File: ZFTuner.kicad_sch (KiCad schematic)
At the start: 2 parts, among them J101 RF_In, J102 RF_Out

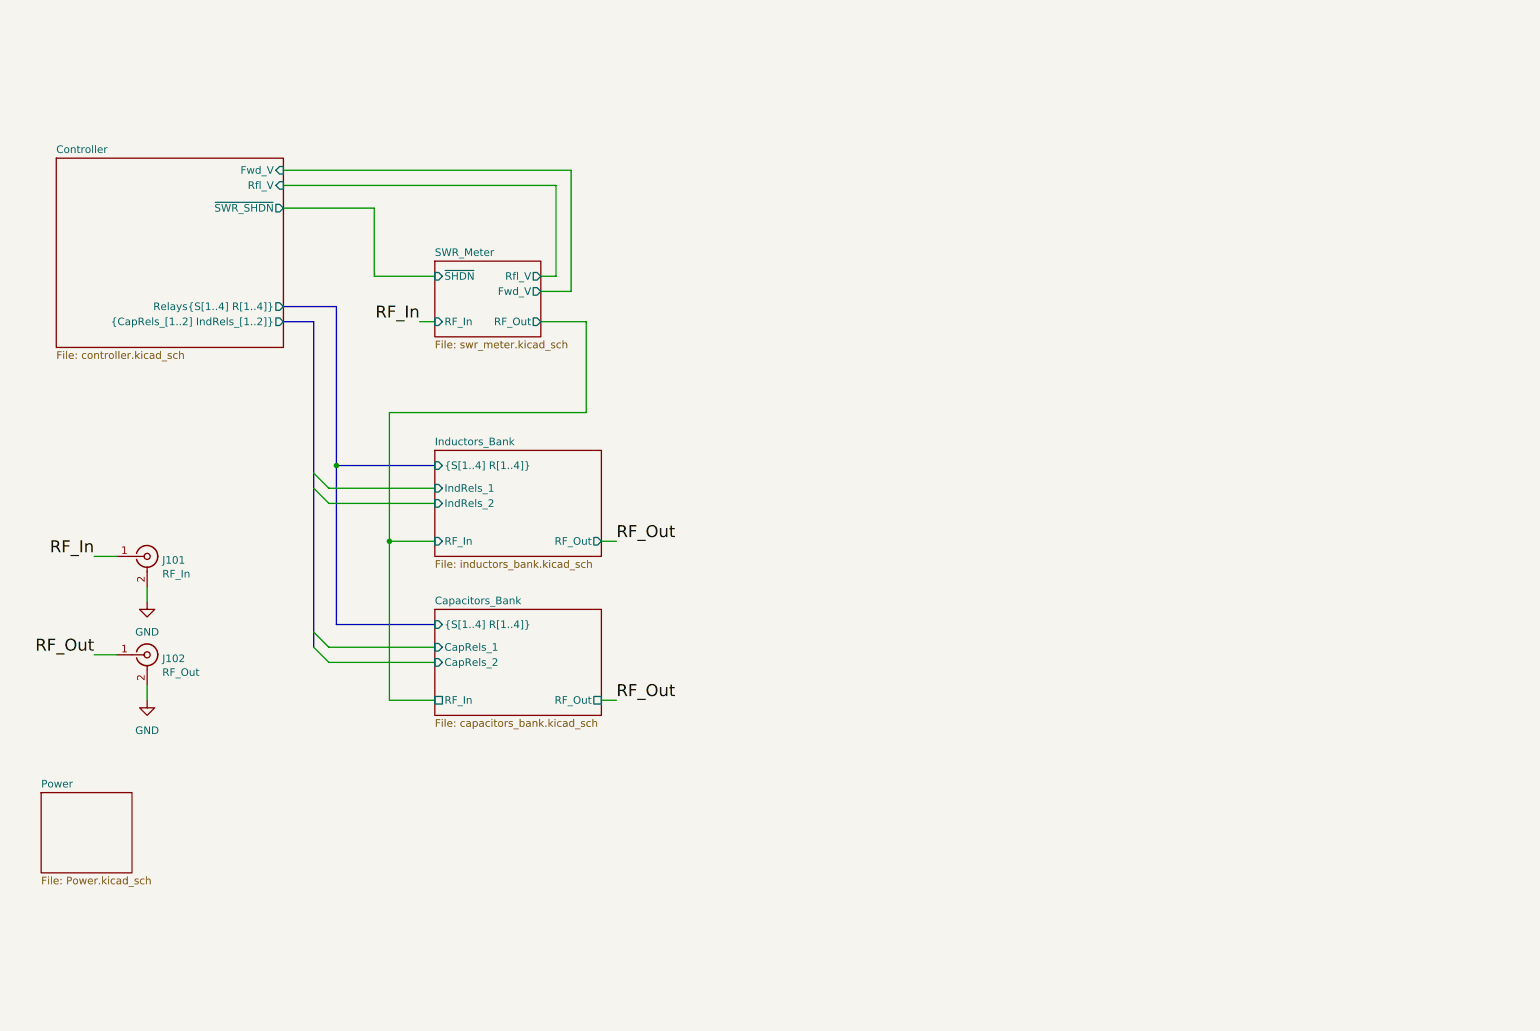
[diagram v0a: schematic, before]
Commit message: Add some missing footprints and rearranged schematics a bit
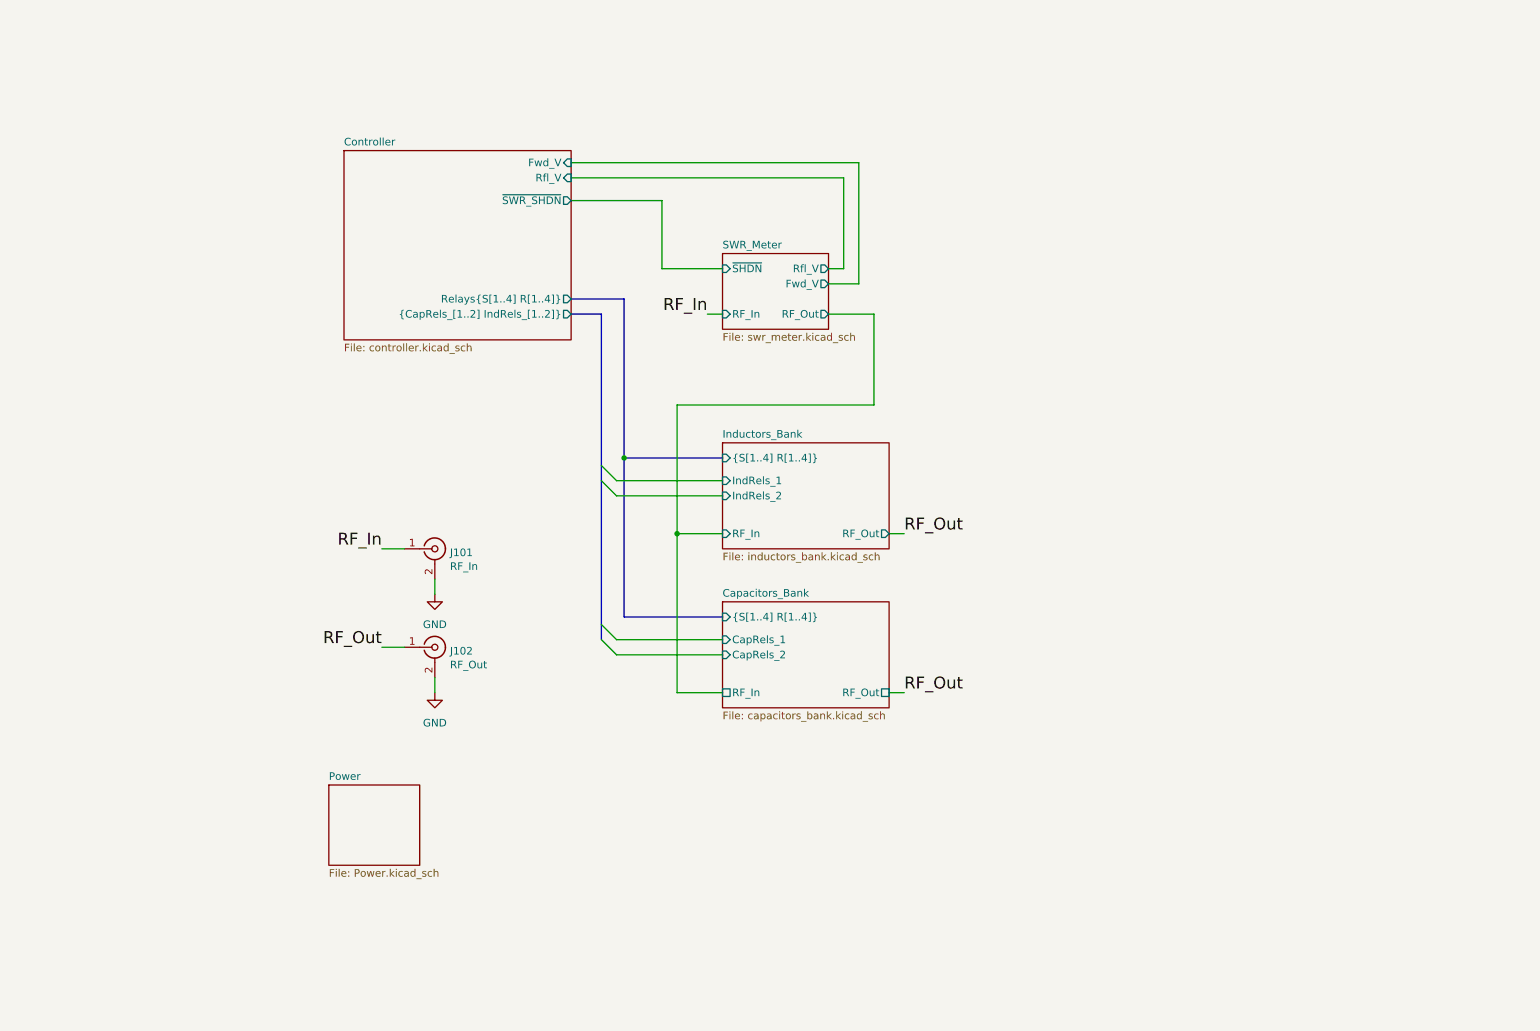
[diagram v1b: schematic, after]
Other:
- moved on the sheet: J101, J102

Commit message: Added connectors to top schematic. Added xtal and optocouplers to controller.
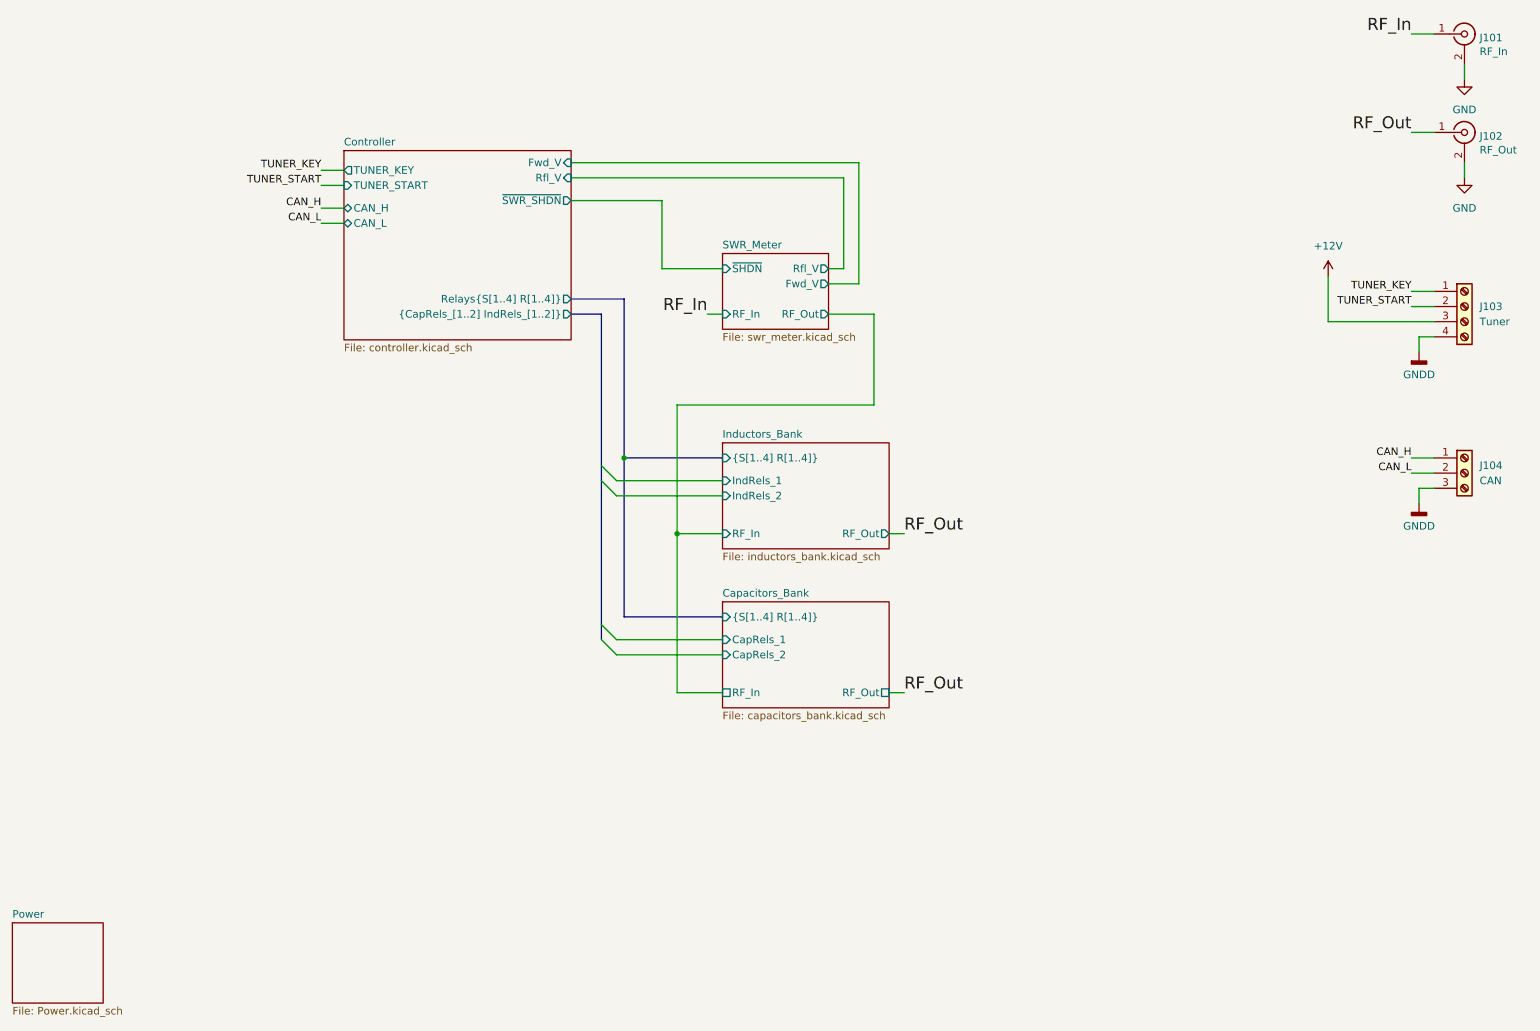
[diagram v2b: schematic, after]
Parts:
- added J103: Tuner, TerminalBlock_Phoenix:TerminalBlock_Phoenix_PT-1,5-4-3.5-H_1x04_P3.50mm_Horizontal, symbol Connector:Screw_Terminal_01x04
- added J104: CAN, TerminalBlock_Phoenix:TerminalBlock_Phoenix_PT-1,5-3-3.5-H_1x03_P3.50mm_Horizontal, symbol Connector:Screw_Terminal_01x03
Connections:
- new net +12V: J103.3 (Pin_3)
- new net CAN_H: J104.1 (Pin_1)
- new net CAN_L: J104.2 (Pin_2)
- new net GNDD: J103.4 (Pin_4), J104.3 (Pin_3)
- new net TUNER_KEY: J103.1 (Pin_1)
- new net TUNER_START: J103.2 (Pin_2)
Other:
- sheet Controller ports: added CAN_H, CAN_L, TUNER_KEY, TUNER_START; removed none
- moved on the sheet: J101, J102

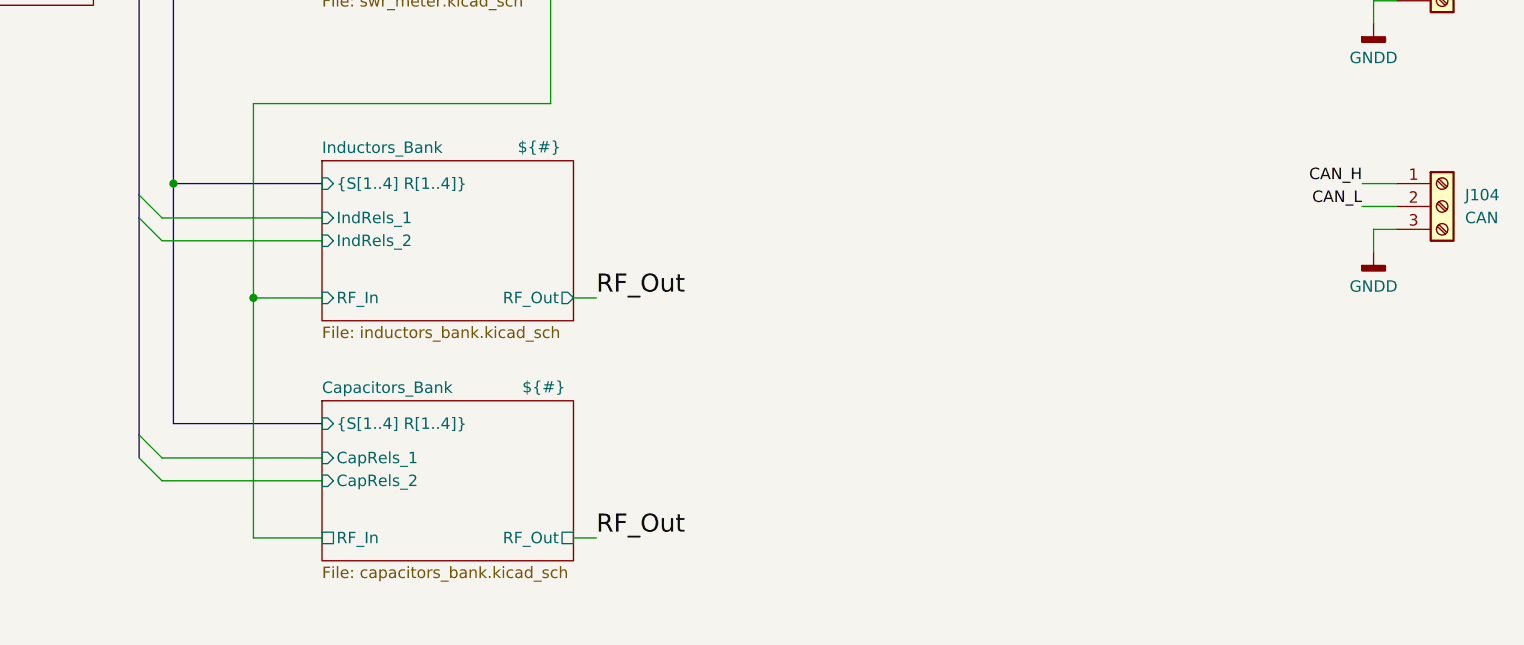
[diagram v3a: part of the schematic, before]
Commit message: Schematic fixes for PCB layout
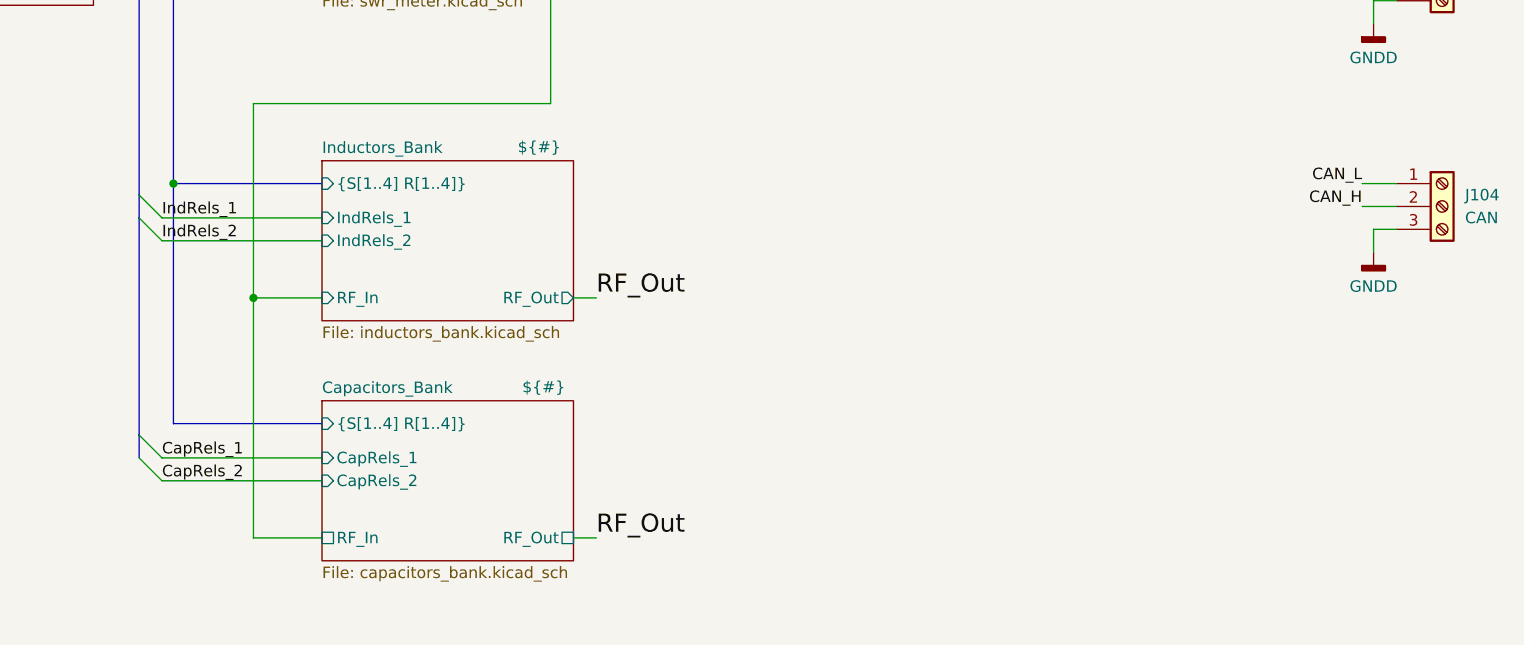
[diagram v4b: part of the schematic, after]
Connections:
- net CAN_H: now also J104.2 (Pin_2); no longer J104.1 (Pin_1)
- net CAN_L: now also J104.1 (Pin_1); no longer J104.2 (Pin_2)
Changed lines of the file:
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@@
+		)
+	)
+	(label "CapRels_2"
+		(at 121.92 129.54 0)
+		(fields_autoplaced yes)
+		(effects
+			(font
+				(size 1.27 1.27)
+			)
+			(justify left bottom)
 		)
 	)
@@
 			(font
 				(size 2.0066 2.0066)
+			)
+			(justify left bottom)
+		)
+	)
+	(label "CapRels_1"
+		(at 121.92 127 0)
+		(fields_autoplaced yes)
+		(effects
+			(font
+				(size 1.27 1.27)
 			)
 			(justify left bottom)
@@
 			)
 			(justify right bottom)
+		)
+	)
+	(label "IndRels_1"
+		(at 121.92 100.33 0)
+		(fields_autoplaced yes)
+		(effects
+			(font
+				(size 1.27 1.27)
+			)
+			(justify left bottom)
 		)
 	)
@@
 	)
 	(label "CAN_L"
-		(at 255.27 99.06 180)
+		(at 255.27 96.52 180)
 		(fields_autoplaced yes)
 		(effects
@@
 	)
 	(label "CAN_H"
-		(at 255.27 96.52 180)
+		(at 255.27 99.06 180)
 		(fields_autoplaced yes)
 		(effects
@@
 		)
 	)
+	(label "IndRels_2"
+		(at 121.92 102.87 0)
+		(fields_autoplaced yes)
+		(effects
+			(font
+				(size 1.27 1.27)
+			)
+			(justify left bottom)
+		)
+	)
